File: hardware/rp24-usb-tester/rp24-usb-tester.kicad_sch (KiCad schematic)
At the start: 40 parts, among them J1 SPEAKER, J2 POWER, J3 EXT_CAP, J4 505070-2422, J5 RAILS, J6 AUX, J7 MOTOR, P1 USB_C_Receptacle_USB2.0_16P, Q1 SS8050, Q2 SS8050, Q3 SS8050, Q4 SS8050, Q5 SS8050, U1 MT2492

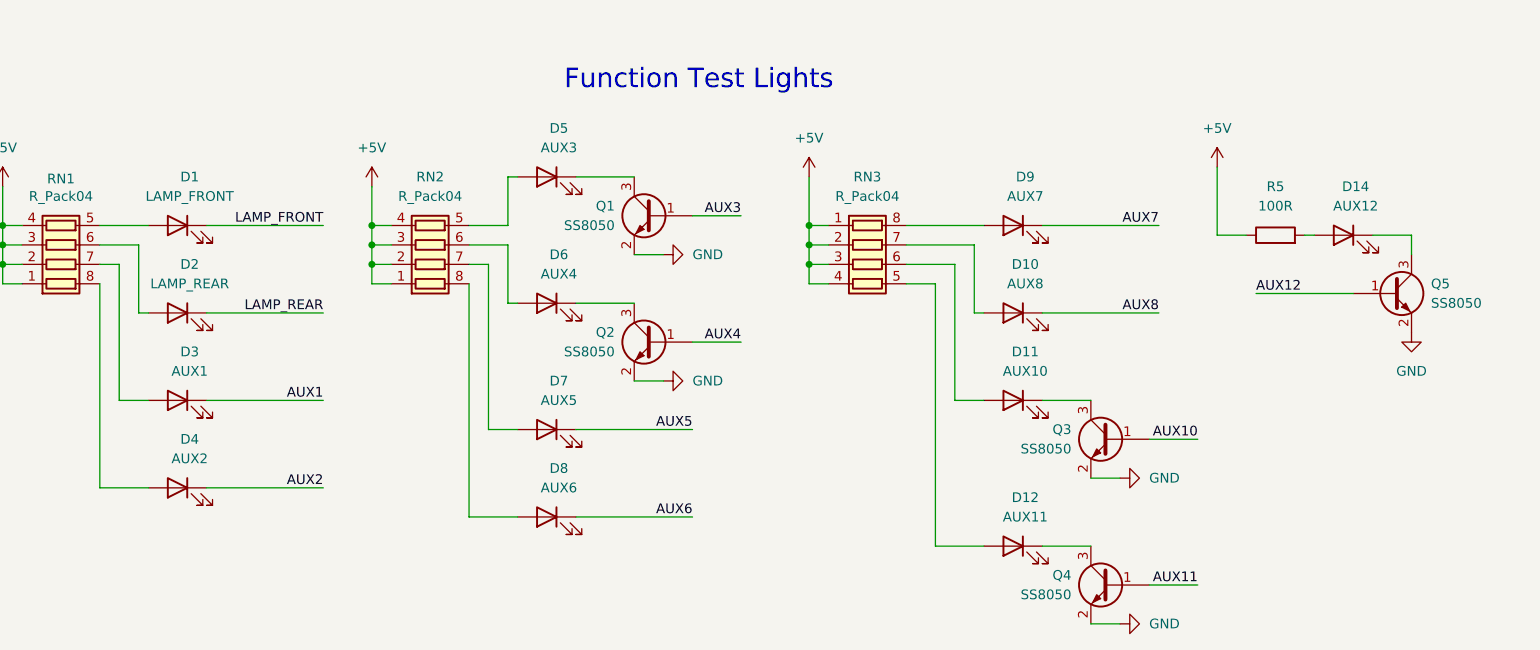
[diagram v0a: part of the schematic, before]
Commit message: chore: rename leds to avoid jlcpcb warnings
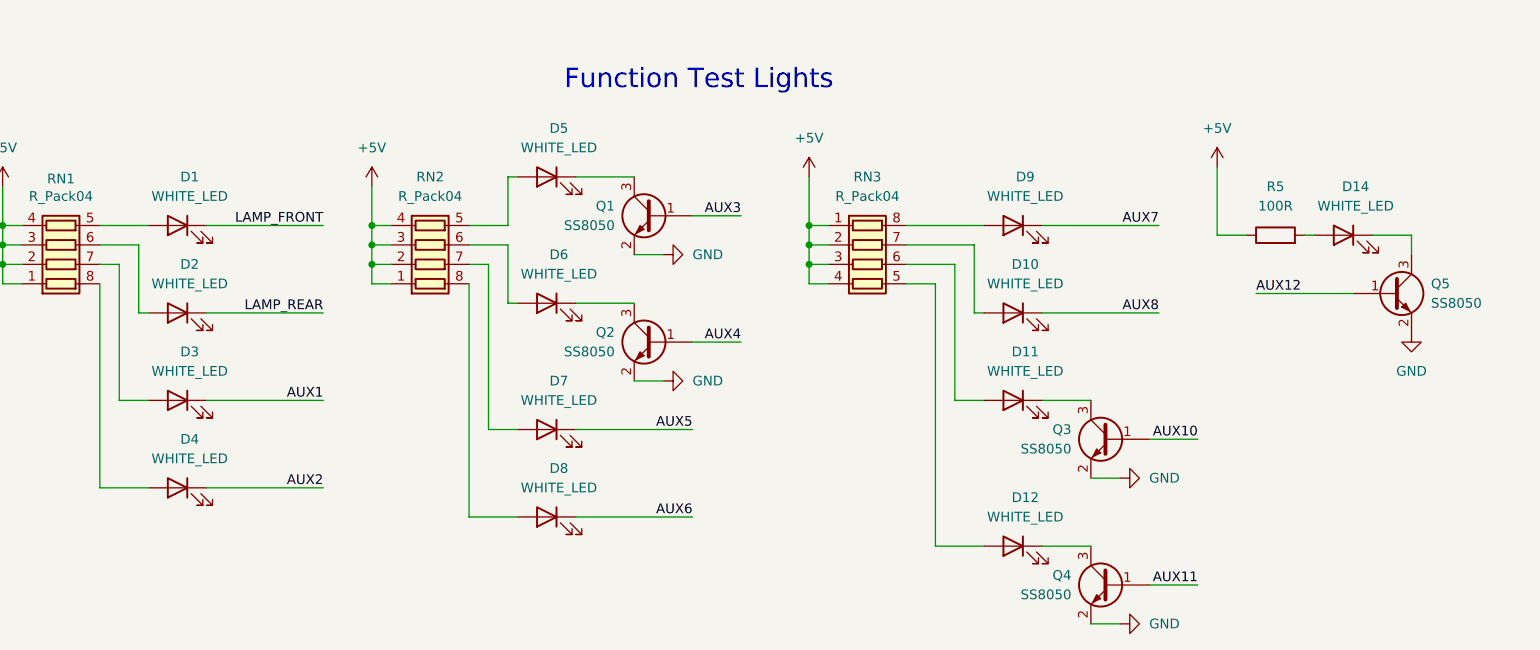
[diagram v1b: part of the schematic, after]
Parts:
- D1: value LAMP_FRONT -> WHITE_LED
- D10: value AUX8 -> WHITE_LED
- D11: value AUX10 -> WHITE_LED
- D12: value AUX11 -> WHITE_LED
- D14: value AUX12 -> WHITE_LED
- D2: value LAMP_REAR -> WHITE_LED
- D3: value AUX1 -> WHITE_LED
- D4: value AUX2 -> WHITE_LED
- D5: value AUX3 -> WHITE_LED
- D6: value AUX4 -> WHITE_LED
- D7: value AUX5 -> WHITE_LED
- D8: value AUX6 -> WHITE_LED
- D9: value AUX7 -> WHITE_LED
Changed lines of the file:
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@@
 			)
 		)
-		(property "Value" "AUX1"
+		(property "Value" "WHITE_LED"
 			(at 39.6875 144.78 0)
 			(effects
@@
 			)
 		)
-		(property "Value" "AUX3"
+		(property "Value" "WHITE_LED"
 			(at 87.9475 115.57 0)
 			(effects
@@
 			)
 		)
-		(property "Value" "AUX12"
+		(property "Value" "WHITE_LED"
 			(at 192.0875 123.19 0)
 			(effects
@@
 			)
 		)
-		(property "Value" "AUX10"
+		(property "Value" "WHITE_LED"
 			(at 148.9075 144.78 0)
 			(effects
@@
 			)
 		)
-		(property "Value" "AUX2"
+		(property "Value" "WHITE_LED"
 			(at 39.6875 156.21 0)
 			(effects
@@
 			)
 		)
-		(property "Value" "LAMP_FRONT"
+		(property "Value" "WHITE_LED"
 			(at 39.6875 121.92 0)
 			(effects
@@
 			)
 		)
-		(property "Value" "AUX4"
+		(property "Value" "WHITE_LED"
 			(at 87.9475 132.08 0)
 			(effects
@@
 			)
 		)
-		(property "Value" "AUX7"
+		(property "Value" "WHITE_LED"
 			(at 148.9075 121.92 0)
 			(effects
@@
 			)
 		)
-		(property "Value" "AUX5"
+		(property "Value" "WHITE_LED"
 			(at 87.9475 148.59 0)
 			(effects
@@
 			)
 		)
-		(property "Value" "AUX8"
+		(property "Value" "WHITE_LED"
 			(at 148.9075 133.35 0)
 			(effects
@@
 			)
 		)
-		(property "Value" "LAMP_REAR"
+		(property "Value" "WHITE_LED"
 			(at 39.6875 133.35 0)
 			(effects
@@
 			)
 		)
-		(property "Value" "AUX6"
+		(property "Value" "WHITE_LED"
 			(at 87.9475 160.02 0)
 			(effects
@@
 			)
 		)
-		(property "Value" "AUX11"
+		(property "Value" "WHITE_LED"
 			(at 148.9075 163.83 0)
 			(effects
